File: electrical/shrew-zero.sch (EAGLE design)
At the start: 44 parts, among them IC1 LMR16006YQ3DDCTQ1, U1 ESP32-PICO-D4, U2 SX1280IMLTRT, X5 PIN-1X-BIG, X6 PIN-1X-BIG, Y1 52MHz TCXO

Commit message: sorted component ref des
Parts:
- removed C25: 10u, shrew-common:CAP0805
- removed C26: 100n, shrew-common:CAP0402-REV
- removed EDGE1: (no value), shrew-common:M05PTH
- removed FL1: 2450FM07D0034T, shrew-core:2450FM07D0034T
- removed X5, X6: PIN-1X-BIG, shrew-core:PIN-1X-BIG
- added C15, C24: 470n, shrew-common:CAP0402-REV
- added JP2: (no value), shrew-common:M04-CLEAN
- added X1, X2: PIN-1X-BIG, shrew-core:PIN-1X-BIG
- added Y2: 52MHz TCXO, shrew-common:OSCILLATOR-TG2016SMN
- C1: value 1n -> 100n
- C10, C5, C6, C7, C8, C9: value 100n -> 10u; device shrew-common:CAP0402-REV -> shrew-common:CAP0805
- C11: value 10uF 25V -> 100n; device shrew-common:CAP0805 -> shrew-common:CAP0402-REV
- C12: value DNP -> 100n; device shrew-common:CAP0402-CAP -> shrew-common:CAP0402-REV
- C13: value 470n -> 100n
- C14: value 10u -> 10uF 25V
- C16: value 10u -> DNP; device shrew-common:CAP0805 -> shrew-common:CAP0402-CAP
- C18, C19: value 10u -> 10n; device shrew-common:CAP0805 -> shrew-common:CAP0402-REV
- C2: value 470n -> 10u; device shrew-common:CAP0402-REV -> shrew-common:CAP0805
- C20: value 10u -> 1n; device shrew-common:CAP0805 -> shrew-common:CAP0402-REV
- C21, C22, C23: value 10u -> 100n; device shrew-common:CAP0805 -> shrew-common:CAP0402-REV
- C3, C4: value 10n -> 10u; device shrew-common:CAP0402-REV -> shrew-common:CAP0805
- D1: value 3V6 -> (none); device shrew-common:DIODE-ZENER-BZT52 -> shrew-common:DIODESOD
- D2: value (none) -> 3V6; device shrew-common:DIODESOD -> shrew-common:DIODE-ZENER-BZT52
- JP1: device shrew-common:M04-CLEAN -> shrew-common:M05PTH
- L1: value 15u -> 6u8
- L2: value 6u8 -> 15u
- R2: value 10K -> 68K
- R4: value 68K -> 10K
- Y1: value 52MHz TCXO -> 2450FM07D0034001T; device shrew-common:OSCILLATOR-TG2016SMN -> shrew-core:2450FM07D0034T
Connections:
- net +24V: now also C10.1, C3.1, C4.1, C5.1, C6.1, C7.1, C8.1, C9.1, R2.2, X1.P$1; no longer C14.1, C16.1, C18.1, C19.1, C20.1, C21.1, C22.1, C23.1, R4.2, X5.P$1
- net 3.3V: now also C12.1, C13.1, C14.1, C2.1, C21.2, C22.2, C23.2, L1.2, Y2.VCC; no longer C10.1, C25.1, C5.2, C6.2, C7.2, C8.1, C9.1, L2.2, Y1.VCC
- net AUX1: now also JP1.1; no longer EDGE1.1
- net AUX2: now also JP1.2; no longer EDGE1.2
- net BATT-ADC: now also D2.C, R4.2; no longer D1.C, R2.2
- net ESP-BOOT: now also C16.2; no longer C12.2
- net ESP-EN: now also C15.2; no longer C13.2
- net GND: now also C12.2, C13.2, C15.1, C16.1, C18.1, C19.1, C2.2, C21.1, C22.1, C23.1, C24.1, C3.2, C4.2, C5.2, C6.2, C7.2, JP1.5, R4.1, X2.P$1, Y2.GND; no longer C12.1, C13.1, C16.2, C18.2, C19.2, C2.1, C20.2, C21.2, C22.2, C23.2, C25.2, C3.1, C4.1, C5.1, C6.1, C7.1, EDGE1.5, R2.1, X6.P$1, Y1.GND
- net N$10: now also C1.1, D1.C, L1.1; no longer C26.1, D2.C, L2.1
- net N$11: now also C19.2; no longer C3.2
- net N$2: now also C20.1, Y2.OUT; no longer C1.1, Y1.OUT
- net N$3: now also C20.2; no longer C1.2
- net N$4: now also C1.2; no longer C26.2
- net N$6: now also Y1.IN; no longer FL1.IN
- net N$7: now also Y1.OUT; no longer FL1.OUT
- net N$9: now also L2.2; no longer L1.2
- net RADIO-VDD: now also C18.2, C24.2, L2.1; no longer C2.2, C4.2, L1.1
- net SIG1: now also JP2.1; no longer JP1.1
- net SIG2: now also JP2.2; no longer JP1.2
- net SIG3: now also JP2.3; no longer JP1.3
- net SIG4: now also JP2.4; no longer JP1.4
- net U0RXD: now also JP1.3; no longer EDGE1.3
- net U0TXD: now also JP1.4; no longer EDGE1.4
- net V-ADC: now also R2.1; no longer R4.1
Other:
- moved on the sheet: ANT2, C1, C10, C11, C12, C13, C14, C16, C18, C19, C2, C20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

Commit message: shrew zero layout improvements
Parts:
- removed D2: 3V6, shrew-common:DIODE-ZENER-BZT52
- added C25, C26: 470n, shrew-common:CAP0402-REV
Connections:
- net 3.3V: now also C25.1, C26.1
- net BATT-ADC: no longer D2.C
- net GND: now also C25.2, C26.2; no longer D2.A
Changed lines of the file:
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@@
 <part name="P+8" library="shrew-common" deviceset="3.3V" device=""/>
 <part name="GND13" library="shrew-common" deviceset="GND" device=""/>
-<part name="D2" library="shrew-common" deviceset="DIODE-ZENER" device="-BZT52" value="3V6"/>
 <part name="R4" library="shrew-common" deviceset="RESISTOR" device="0402-REV" value="10K"/>
 <part name="R3" library="shrew-common" deviceset="RESISTOR" device="0402-REV" value="10K"/>
@@
 <part name="JP2" library="shrew-common" deviceset="M04" device="-CLEAN"/>
 <part name="C10" library="shrew-common" deviceset="CAP" device="0805" value="10u"/>
+<part name="C25" library="shrew-common" deviceset="CAP" device="0402-REV" value="470n"/>
+<part name="C26" library="shrew-common" deviceset="CAP" device="0402-REV" value="470n"/>
+<part name="P+13" library="shrew-common" deviceset="3.3V" device=""/>
+<part name="GND26" library="shrew-common" deviceset="GND" device=""/>
 </parts>
 <sheets>
@@
 <instance part="P+8" gate="G$1" x="104.14" y="-2.54"/>
 <instance part="GND13" gate="1" x="104.14" y="-20.32"/>
-<instance part="D2" gate="G$1" x="43.18" y="-63.5" rot="R90"/>
 <instance part="R4" gate="G$1" x="50.8" y="-60.96" rot="R90"/>
 <instance part="R3" gate="G$1" x="50.8" y="-45.72" rot="R90"/>
@@
 <attribute name="NAME" x="232.664" y="165.481" size="1.778" layer="95"/>
 </instance>
+<instance part="C25" gate="G$1" x="78.74" y="-63.5"/>
+<instance part="C26" gate="G$1" x="88.9" y="-63.5"/>
+<instance part="P+13" gate="G$1" x="78.74" y="-53.34"/>
+<instance part="GND26" gate="1" x="78.74" y="-73.66"/>
 </instances>
 <busses>
@@
 </segment>
 <segment>
-<pinref part="D2" gate="G$1" pin="A"/>
-<wire x1="43.18" y1="-66.04" x2="43.18" y2="-68.58" width="0.1524" layer="91"/>
-<wire x1="43.18" y1="-68.58" x2="50.8" y2="-68.58" width="0.1524" layer="91"/>
 <pinref part="R4" gate="G$1" pin="1"/>
 <wire x1="50.8" y1="-68.58" x2="50.8" y2="-66.04" width="0.1524" layer="91"/>
@@
 <wire x1="50.8" y1="-68.58" x2="50.8" y2="-71.12" width="0.1524" layer="91"/>
 <pinref part="C17" gate="G$1" pin="2"/>
-<wire x1="43.18" y1="-68.58" x2="30.48" y2="-68.58" width="0.1524" layer="91"/>
+<wire x1="50.8" y1="-68.58" x2="30.48" y2="-68.58" width="0.1524" layer="91"/>
 <wire x1="30.48" y1="-68.58" x2="30.48" y2="-63.5" width="0.1524" layer="91"/>
-<junction x="43.18" y="-68.58"/>
 <junction x="50.8" y="-68.58"/>
 </segment>
@@
 <wire x1="68.58" y1="165.1" x2="66.04" y2="165.1" width="0.1524" layer="91"/>
 <wire x1="66.04" y1="165.1" x2="66.04" y2="162.56" width="0.1524" layer="91"/>
+</segment>
+<segment>
+<pinref part="GND26" gate="1" pin="GND"/>
+<pinref part="C25" gate="G$1" pin="2"/>
+<wire x1="78.74" y1="-71.12" x2="78.74" y2="-68.58" width="0.1524" layer="91"/>
+<pinref part="C26" gate="G$1" pin="2"/>
+<wire x1="78.74" y1="-68.58" x2="78.74" y2="-66.04" width="0.1524" layer="91"/>
+<wire x1="78.74" y1="-68.58" x2="88.9" y2="-68.58" width="0.1524" layer="91"/>
+<wire x1="88.9" y1="-68.58" x2="88.9" y2="-66.04" width="0.1524" layer="91"/>
+<junction x="78.74" y="-68.58"/>
 </segment>
 </net>
@@
 <pinref part="C2" gate="G$1" pin="1"/>
 </segment>
+<segment>
+<pinref part="P+13" gate="G$1" pin="3.3V"/>
+<pinref part="C25" gate="G$1" pin="1"/>
+<wire x1="78.74" y1="-53.34" x2="78.74" y2="-55.88" width="0.1524" layer="91"/>
+<pinref part="C26" gate="G$1" pin="1"/>
+<wire x1="78.74" y1="-55.88" x2="78.74" y2="-58.42" width="0.1524" layer="91"/>
+<wire x1="78.74" y1="-55.88" x2="88.9" y2="-55.88" width="0.1524" layer="91"/>
+<wire x1="88.9" y1="-55.88" x2="88.9" y2="-58.42" width="0.1524" layer="91"/>
+<junction x="78.74" y="-55.88"/>
+</segment>
 </net>
 <net name="U0TXD" class="0">
@@
 <pinref part="R4" gate="G$1" pin="2"/>
 <wire x1="50.8" y1="-50.8" x2="50.8" y2="-53.34" width="0.1524" layer="91"/>
-<pinref part="D2" gate="G$1" pin="C"/>
 <wire x1="50.8" y1="-53.34" x2="50.8" y2="-55.88" width="0.1524" layer="91"/>
-<wire x1="43.18" y1="-60.96" x2="43.18" y2="-53.34" width="0.1524" layer="91"/>
-<wire x1="43.18" y1="-53.34" x2="50.8" y2="-53.34" width="0.1524" layer="91"/>
-<wire x1="43.18" y1="-53.34" x2="30.48" y2="-53.34" width="0.1524" layer="91"/>
+<wire x1="50.8" y1="-53.34" x2="30.48" y2="-53.34" width="0.1524" layer="91"/>
 <label x="27.94" y="-53.34" size="1.27" layer="95" rot="R180" xref="yes"/>
 <pinref part="C17" gate="G$1" pin="1"/>
@@
 <wire x1="30.48" y1="-55.88" x2="30.48" y2="-53.34" width="0.1524" layer="91"/>
 <junction x="50.8" y="-53.34"/>
-<junction x="43.18" y="-53.34"/>
 <junction x="30.48" y="-53.34"/>
 </segment>

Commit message: shrew zero next prototype ready to mfg
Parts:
- added C27: 100n, shrew-common:CAP0402-REV
- added C28: 0p5, shrew-common:CAP0402-REV
- ANT1, ANT2: value 74889302450 -> ANT3216LL00R2400A
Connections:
- net 3.3V: now also C27.2
- net GND: now also C27.1, C28.1
- net N$1: now also C28.2
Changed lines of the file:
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@@
 <part name="R1" library="shrew-common" deviceset="RESISTOR" device="0402-REV" value="10K"/>
 <part name="P+7" library="shrew-common" deviceset="3.3V" device=""/>
-<part name="ANT1" library="shrew-common" deviceset="ANTENNA2" device="SMD" value="74889302450"/>
+<part name="ANT1" library="shrew-common" deviceset="ANTENNA2" device="SMD" value="ANT3216LL00R2400A"/>
 <part name="Y1" library="shrew-core" deviceset="2450FM07D0034T" device="" value="2450FM07D0034001T"/>
-<part name="ANT2" library="shrew-common" deviceset="ANTENNA2" device="SMD" value="74889302450"/>
+<part name="ANT2" library="shrew-common" deviceset="ANTENNA2" device="SMD" value="ANT3216LL00R2400A"/>
 <part name="C20" library="shrew-common" deviceset="CAP" device="0402-REV" value="1n"/>
 <part name="GND20" library="shrew-common" deviceset="GND" device=""/>
@@
 <part name="P+13" library="shrew-common" deviceset="3.3V" device=""/>
 <part name="GND26" library="shrew-common" deviceset="GND" device=""/>
+<part name="C27" library="shrew-common" deviceset="CAP" device="0402-REV" value="100n"/>
+<part name="C28" library="shrew-common" deviceset="CAP" device="0402-REV" value="0p5"/>
+<part name="GND27" library="shrew-common" deviceset="GND" device=""/>
 </parts>
 <sheets>
@@
 <instance part="GND24" gate="1" x="345.44" y="35.56"/>
 <instance part="C21" gate="G$1" x="193.04" y="66.04" rot="R180"/>
-<instance part="GND21" gate="1" x="193.04" y="55.88"/>
+<instance part="GND21" gate="1" x="193.04" y="50.8"/>
 <instance part="C12" gate="G$1" x="142.24" y="104.14"/>
 <instance part="C13" gate="G$1" x="154.94" y="104.14"/>
@@
 <instance part="P+13" gate="G$1" x="78.74" y="-53.34"/>
 <instance part="GND26" gate="1" x="78.74" y="-73.66"/>
+<instance part="C27" gate="G$1" x="182.88" y="66.04" rot="R180"/>
+<instance part="C28" gate="G$1" x="142.24" y="63.5" rot="R270"/>
+<instance part="GND27" gate="1" x="149.86" y="58.42"/>
 </instances>
 <busses>
@@
 <pinref part="GND21" gate="1" pin="GND"/>
 <wire x1="193.04" y1="60.96" x2="193.04" y2="58.42" width="0.1524" layer="91"/>
+<pinref part="C27" gate="G$1" pin="1"/>
+<wire x1="193.04" y1="58.42" x2="193.04" y2="53.34" width="0.1524" layer="91"/>
+<wire x1="182.88" y1="60.96" x2="182.88" y2="58.42" width="0.1524" layer="91"/>
+<wire x1="182.88" y1="58.42" x2="193.04" y2="58.42" width="0.1524" layer="91"/>
+<junction x="193.04" y="58.42"/>
 </segment>
 <segment>
@@
 <wire x1="231.14" y1="160.02" x2="231.14" y2="157.48" width="0.1524" layer="91"/>
 <wire x1="231.14" y1="157.48" x2="220.98" y2="157.48" width="0.1524" layer="91"/>
+<junction x="220.98" y="157.48"/>
 </segment>
 <segment>
@@
 <wire x1="88.9" y1="-68.58" x2="88.9" y2="-66.04" width="0.1524" layer="91"/>
 <junction x="78.74" y="-68.58"/>
+</segment>
+<segment>
+<pinref part="C28" gate="G$1" pin="1"/>
+<pinref part="GND27" gate="1" pin="GND"/>
+<wire x1="147.32" y1="63.5" x2="149.86" y2="63.5" width="0.1524" layer="91"/>
+<wire x1="149.86" y1="63.5" x2="149.86" y2="60.96" width="0.1524" layer="91"/>
 </segment>
 </net>
@@
 <wire x1="193.04" y1="76.2" x2="193.04" y2="78.74" width="0.1524" layer="91"/>
 <pinref part="C21" gate="G$1" pin="2"/>
-<wire x1="193.04" y1="68.58" x2="193.04" y2="76.2" width="0.1524" layer="91"/>
+<wire x1="193.04" y1="68.58" x2="193.04" y2="71.12" width="0.1524" layer="91"/>
 <junction x="193.04" y="76.2"/>
+<pinref part="C27" gate="G$1" pin="2"/>
+<wire x1="193.04" y1="71.12" x2="193.04" y2="76.2" width="0.1524" layer="91"/>
+<wire x1="182.88" y1="68.58" x2="182.88" y2="71.12" width="0.1524" layer="91"/>
+<wire x1="182.88" y1="71.12" x2="193.04" y2="71.12" width="0.1524" layer="91"/>
+<junction x="193.04" y="71.12"/>
 </segment>
 <segment>
@@
 <wire x1="111.76" y1="66.04" x2="134.62" y2="66.04" width="0.1524" layer="91"/>
 <wire x1="134.62" y1="66.04" x2="134.62" y2="68.58" width="0.1524" layer="91"/>
+<pinref part="C28" gate="G$1" pin="2"/>
+<wire x1="139.7" y1="63.5" x2="134.62" y2="63.5" width="0.1524" layer="91"/>
+<wire x1="134.62" y1="63.5" x2="134.62" y2="66.04" width="0.1524" layer="91"/>
+<junction x="134.62" y="66.04"/>
 </segment>
 </net>
@@
 <wire x1="220.98" y1="170.18" x2="231.14" y2="170.18" width="0.1524" layer="91"/>
 <wire x1="231.14" y1="170.18" x2="231.14" y2="167.64" width="0.1524" layer="91"/>
-</segment>
-<segment>
+<junction x="220.98" y="170.18"/>
+</segment>
+<segment>

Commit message: PCB changes for better EMI emissions
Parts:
- added C29: 470n, shrew-common:CAP0402-REV
- added C30: DNP, shrew-common:CAP0402-CAP
- C11: value 100n -> 10u; device shrew-common:CAP0402-REV -> shrew-common:CAP0805
- C14: value 10uF 25V -> 100n; device shrew-common:CAP0805 -> shrew-common:CAP0402-REV
- C15, C17, C25, C26: value 470n -> 100n
- C16: value DNP -> 100n; device shrew-common:CAP0402-CAP -> shrew-common:CAP0402-REV
- C18: value 10n -> 10uF 25V; device shrew-common:CAP0402-REV -> shrew-common:CAP0805
- C20: value 1n -> 10n
- C21: value 100n -> 1n
- C22, C27: value 100n -> 470n
- C24: value 470n -> 0p5
- C28: value 0p5 -> 100n
- C3: value 10u -> 470n; device shrew-common:CAP0805 -> shrew-common:CAP0402-REV
- U1: value ESP32-PICO-D4 -> SX1280IMLTRT; device shrew-core:ESP32-PICO-D4 -> shrew-core:SX1280IMLTRT
- U2: value SX1280IMLTRT -> ESP32-PICO-D4; device shrew-core:SX1280IMLTRT -> shrew-core:ESP32-PICO-D4
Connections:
- net +24V: now also C11.1; no longer C3.1
- net 3.3V: now also C15.1, C16.1, C17.1, C18.1, C25.2, C26.2, C28.2, C3.1, U1.VBAT, U1.VBAT_IO, U2.VDD3P3_CPU, U2.VDD3P3_RTC, U2.VDDA, U2.VDDA3P3, U2.VDD_SDIO; no longer C11.1, C21.2, C22.2, C25.1, C26.1, C27.2, U1.VDD3P3_CPU, U1.VDD3P3_RTC, U1.VDDA, U1.VDDA3P3, U1.VDD_SDIO, U2.VBAT, U2.VBAT_IO
- net AUX1: now also U2.IO19; no longer U1.IO19
- net AUX2: now also U2.IO22; no longer U1.IO22
- net BATT-ADC: now also C29.1, U2.IO4; no longer C17.1, U1.IO4
- net ESP-BOOT: now also C30.2, U2.IO0(BOOT); no longer C16.2, U1.IO0(BOOT)
- net ESP-EN: now also C22.2, U2.EN; no longer C15.2, U1.EN
- net GND: now also C15.2, C16.2, C18.2, C20.1, C25.1, C26.1, C29.2, C30.1, U1.GND_2, U1.GND_3, U1.GND_4, U1.GND_5, U1.GND_6, U1.GND_7, U2.IO15/MTDO; no longer C15.1, C16.1, C18.1, C21.1, C25.2, C26.2, U1.IO15/MTDO, U2.GND_2, U2.GND_3, U2.GND_4, U2.GND_5, U2.GND_6, U2.GND_7
- net N$1: now also C24.2, U2.LNA_IN; no longer C28.2, U1.LNA_IN
- net N$11: now also C20.2, U1.VR_PA; no longer C19.2, U2.VR_PA
- net N$2: now also C21.1; no longer C20.1
- net N$3: now also C21.2, U1.XTA; no longer C20.2, U2.XTA
- net N$5: now also U2.IO14; no longer U1.IO14
- net N$6: now also U1.RFIO; no longer U2.RFIO
- net N$8: now also U2.IO2; no longer U1.IO2
- net N$9: now also U1.DCC_SW; no longer U2.DCC_SW
- net RADIO-BUSY: now also U1.BUSY, U2.IO23; no longer U1.IO23, U2.BUSY
- net RADIO-CS: now also U1.NSS_CTS, U2.IO32; no longer U1.IO32, U2.NSS_CTS
- net RADIO-DIO: now also U1.DIO1, U2.IO18; no longer U1.IO18, U2.DIO1
- net RADIO-RST: now also U1.NRESET, U2.IO21; no longer U1.IO21, U2.NRESET
- net RADIO-VDD: now also C19.2, C27.2, U1.DCC_FB, U1.VDD_INN; no longer C18.2, C24.2, U2.DCC_FB, U2.VDD_INN
- net RGBLED: now also U2.IO5; no longer U1.IO5
- net SIG1: now also U2.IO13; no longer U1.IO13
- net SIG2: now also U2.IO27; no longer U1.IO27
- net SIG3: now also U2.SD2/IO9; no longer U1.SD2/IO9
- net SIG4: now also U2.SD3/IO10; no longer U1.SD3/IO10
- net SPI-MISO: now also U1.MISO_TX, U2.IO26; no longer U1.IO26, U2.MISO_TX
- net SPI-MOSI: now also U1.MOSI_RX, U2.IO25; no longer U1.IO25, U2.MOSI_RX
- net SPI-SCK: now also U1.SCK_RTSN, U2.IO33; no longer U1.IO33, U2.SCK_RTSN
- net U0RXD: now also U2.U0RXD(IO3); no longer U1.U0RXD(IO3)
- net U0TXD: now also U2.U0TXD(IO1); no longer U1.U0TXD(IO1)
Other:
- moved on the sheet: ANT2, C10, C11, C12, C13, C14, C15, C16, C17, C18, C19, C20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

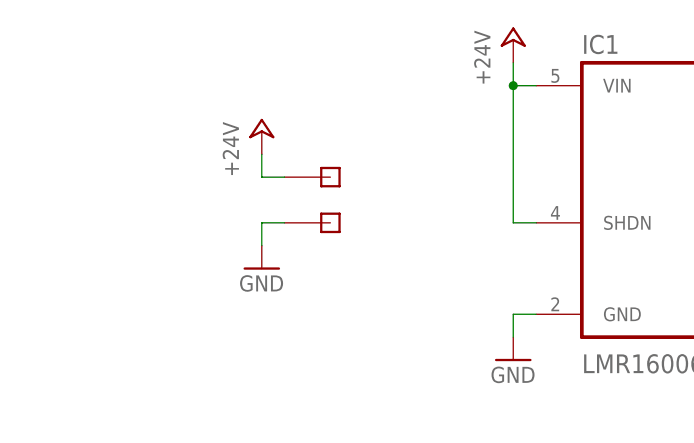
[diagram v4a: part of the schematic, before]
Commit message: shrew zero added reverse protection diode
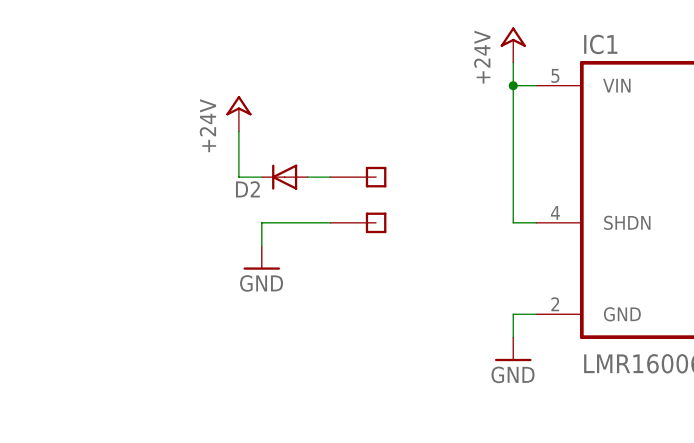
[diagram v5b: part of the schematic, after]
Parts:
- added D2: C406049, shrew-common:DIODESOD
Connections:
- new net N$12: D2.A, X1.P$1
- net +24V: now also D2.C; no longer X1.P$1
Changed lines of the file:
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@@
 <part name="C16" library="shrew-common" deviceset="CAP" device="0402-REV" value="100n"/>
 <part name="GND4" library="shrew-common" deviceset="GND" device=""/>
+<part name="D2" library="shrew-common" deviceset="DIODE" device="SOD" value="C406049"/>
 </parts>
 <sheets>
@@
 <instance part="GND9" gate="1" x="231.14" y="93.98"/>
 <instance part="C30" gate="G$1" x="88.9" y="-60.96" rot="R270"/>
-<instance part="X1" gate="G$1" x="45.72" y="180.34"/>
-<instance part="P+2" gate="1" x="38.1" y="185.42"/>
-<instance part="X2" gate="G$1" x="45.72" y="175.26"/>
+<instance part="X1" gate="G$1" x="50.8" y="180.34"/>
+<instance part="P+2" gate="1" x="35.56" y="187.96"/>
+<instance part="X2" gate="G$1" x="50.8" y="175.26"/>
 <instance part="GND1" gate="1" x="38.1" y="170.18"/>
 <instance part="C4" gate="G$1" x="190.5" y="162.56" smashed="yes">
@@
 <instance part="C16" gate="G$1" x="180.34" y="104.14"/>
 <instance part="GND4" gate="1" x="147.32" y="165.1"/>
+<instance part="D2" gate="G$1" x="40.64" y="180.34" smashed="yes" rot="R180">
+<attribute name="NAME" x="38.1" y="179.8574" size="1.778" layer="95" rot="R180"/>
+</instance>
 </instances>
 <busses>
@@
 <pinref part="X2" gate="G$1" pin="P$1"/>
 <pinref part="GND1" gate="1" pin="GND"/>
-<wire x1="40.64" y1="175.26" x2="38.1" y2="175.26" width="0.1524" layer="91"/>
+<wire x1="45.72" y1="175.26" x2="38.1" y2="175.26" width="0.1524" layer="91"/>
 <wire x1="38.1" y1="175.26" x2="38.1" y2="172.72" width="0.1524" layer="91"/>
 </segment>
@@
 <net name="+24V" class="0">
 <segment>
-<pinref part="X1" gate="G$1" pin="P$1"/>
-<pinref part="P+2" gate="1" pin="+24V"/>
-<wire x1="40.64" y1="180.34" x2="38.1" y2="180.34" width="0.1524" layer="91"/>
-<wire x1="38.1" y1="180.34" x2="38.1" y2="182.88" width="0.1524" layer="91"/>
-</segment>
-<segment>
 <pinref part="P+4" gate="1" pin="+24V"/>
 <pinref part="C4" gate="G$1" pin="1"/>
@@
 <junction x="66.04" y="190.5"/>
 </segment>
+<segment>
+<pinref part="D2" gate="G$1" pin="C"/>
+<wire x1="38.1" y1="180.34" x2="35.56" y2="180.34" width="0.1524" layer="91"/>
+<pinref part="P+2" gate="1" pin="+24V"/>
+<wire x1="35.56" y1="180.34" x2="35.56" y2="185.42" width="0.1524" layer="91"/>
+</segment>
 </net>
 <net name="N$4" class="0">
@@
 </segment>
 </net>
+<net name="N$12" class="0">
+<segment>
+<pinref part="X1" gate="G$1" pin="P$1"/>
+<pinref part="D2" gate="G$1" pin="A"/>
+<wire x1="45.72" y1="180.34" x2="43.18" y2="180.34" width="0.1524" layer="91"/>
+</segment>
+</net>
